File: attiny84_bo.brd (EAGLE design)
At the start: 36 x 20 mm, 11 parts, among them J1 AVR_SPI_PRG_6NS, Y1 16MHz

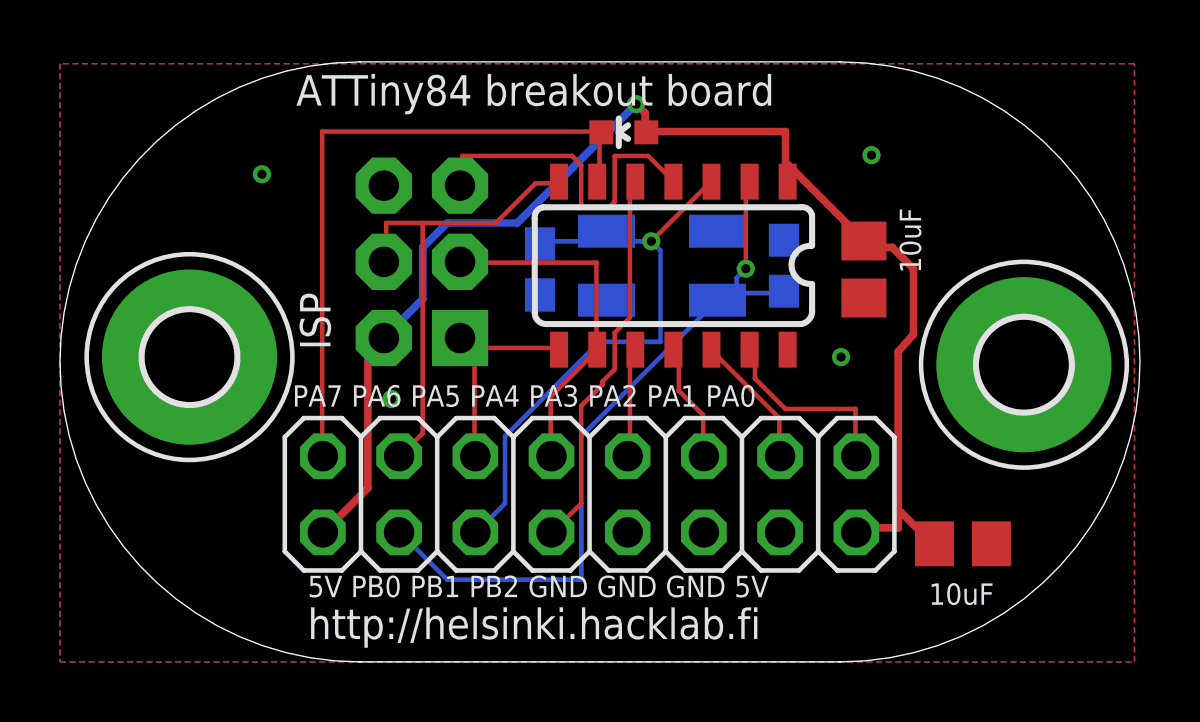
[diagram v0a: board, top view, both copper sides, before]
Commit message: move the other cap near the other 5v input
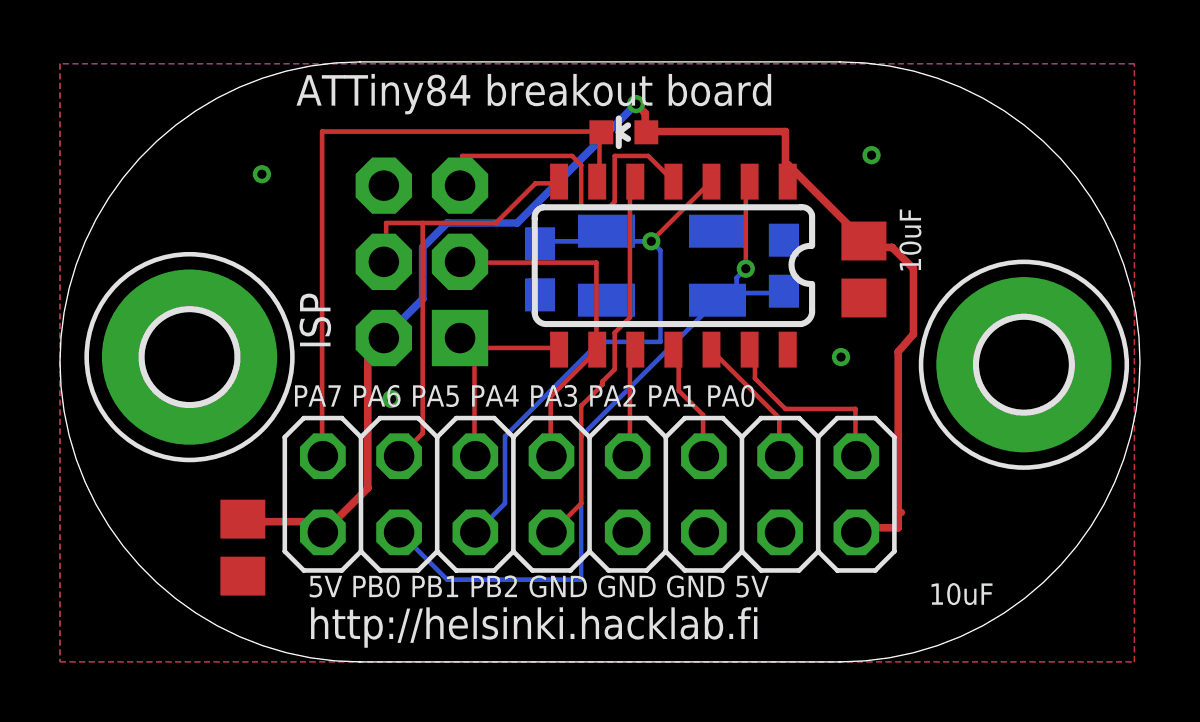
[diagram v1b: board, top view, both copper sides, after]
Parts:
- moved C2 24.0 mm to (6.10, 3.81), turned to 270 degrees
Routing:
- net +5V: track 45.6 -> 47.6 mm
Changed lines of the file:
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@@
 <setting verticaltext="up"/>
 </settings>
-<grid distance="5" unitdist="mil" unit="mil" style="lines" multiple="1" display="yes" altdistance="5" altunitdist="mm" altunit="mm"/>
+<grid distance="5" unitdist="mil" unit="mm" style="lines" multiple="1" display="yes" altdistance="5" altunitdist="mm" altunit="mm"/>
 <layers>
 <layer number="1" name="Top" color="4" fill="1" visible="yes" active="yes"/>
@@
 <attribute name="VALUE" x="19.812" y="18.7325" size="0.4064" layer="27" rot="R180"/>
 </element>
-<element name="C2" library="rcl" package="C0805" value="" x="30.099" y="3.937" smashed="yes">
-<attribute name="VALUE" x="28.829" y="1.397" size="1.27" layer="27"/>
+<element name="C2" library="rcl" package="C0805" value="" x="6.096" y="3.81" smashed="yes" rot="R270">
+<attribute name="VALUE" x="3.556" y="5.08" size="1.27" layer="27" rot="R270"/>
 </element>
 <element name="CX0" library="rcl" package="C0603" value="22pF" x="16.002" y="13.081" smashed="yes" rot="MR90"/>
@@
 <wire x1="19.5072" y1="17.6784" x2="19.546" y2="17.653" width="0.254" layer="1"/>
 <via x="19.2024" y="18.5928" extent="1-16" drill="0.3048"/>
-<wire x1="28.0416" y1="4.9784" x2="29.0576" y2="3.9624" width="0.254" layer="1"/>
-<wire x1="29.0576" y1="3.9624" x2="29.149" y2="3.937" width="0.254" layer="1"/>
 <wire x1="28.0416" y1="4.9784" x2="27.94" y2="4.9784" width="0.254" layer="1"/>
 <contactref element="JP1" pad="16"/>
@@
 <wire x1="10.795" y1="10.795" x2="10.2616" y2="10.2616" width="0.254" layer="1"/>
 <wire x1="8.8392" y1="4.3688" x2="8.763" y2="4.318" width="0.254" layer="1"/>
+<wire x1="9.0424" y1="4.6736" x2="6.096" y2="4.6736" width="0.254" layer="1"/>
+<wire x1="6.096" y1="4.6736" x2="6.096" y2="4.76" width="0.254" layer="1"/>
+<wire x1="9.0424" y1="4.6736" x2="8.763" y2="4.318" width="0.254" layer="1"/>
 </signal>
 <signal name="PB0/XTAL1">
